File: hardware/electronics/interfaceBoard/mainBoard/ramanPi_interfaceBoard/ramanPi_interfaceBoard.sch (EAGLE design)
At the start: 10 parts

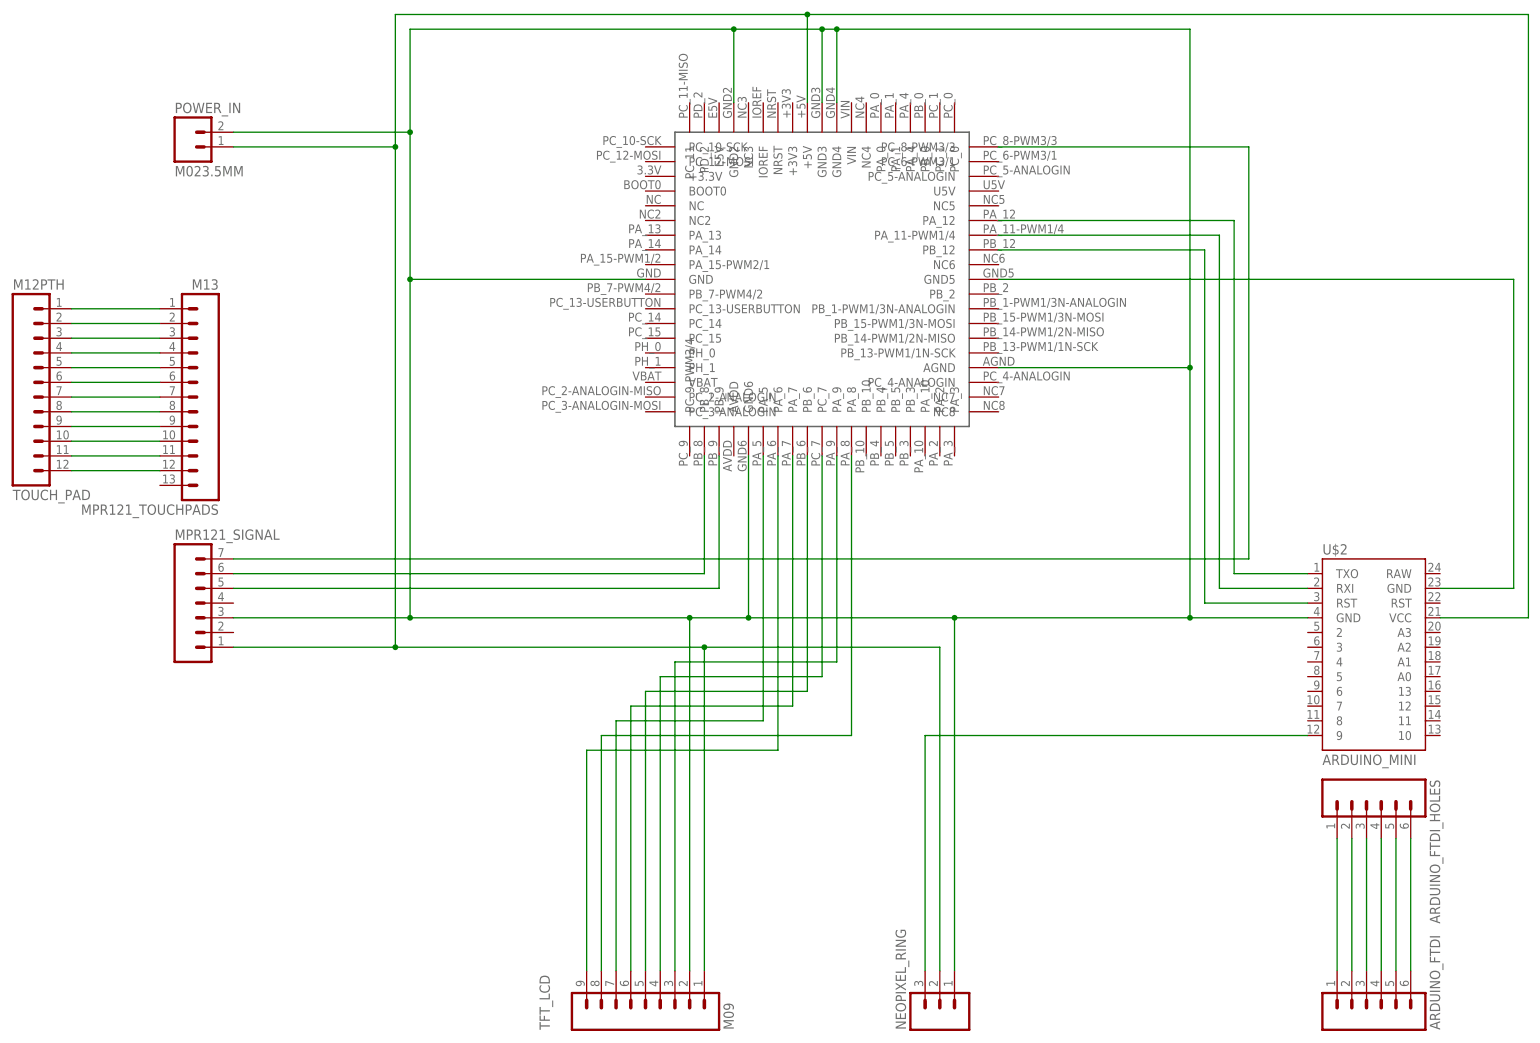
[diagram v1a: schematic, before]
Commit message: added reset circuitry to all stm32 boards
added reset circuitry for raspi to reset each board from remote.
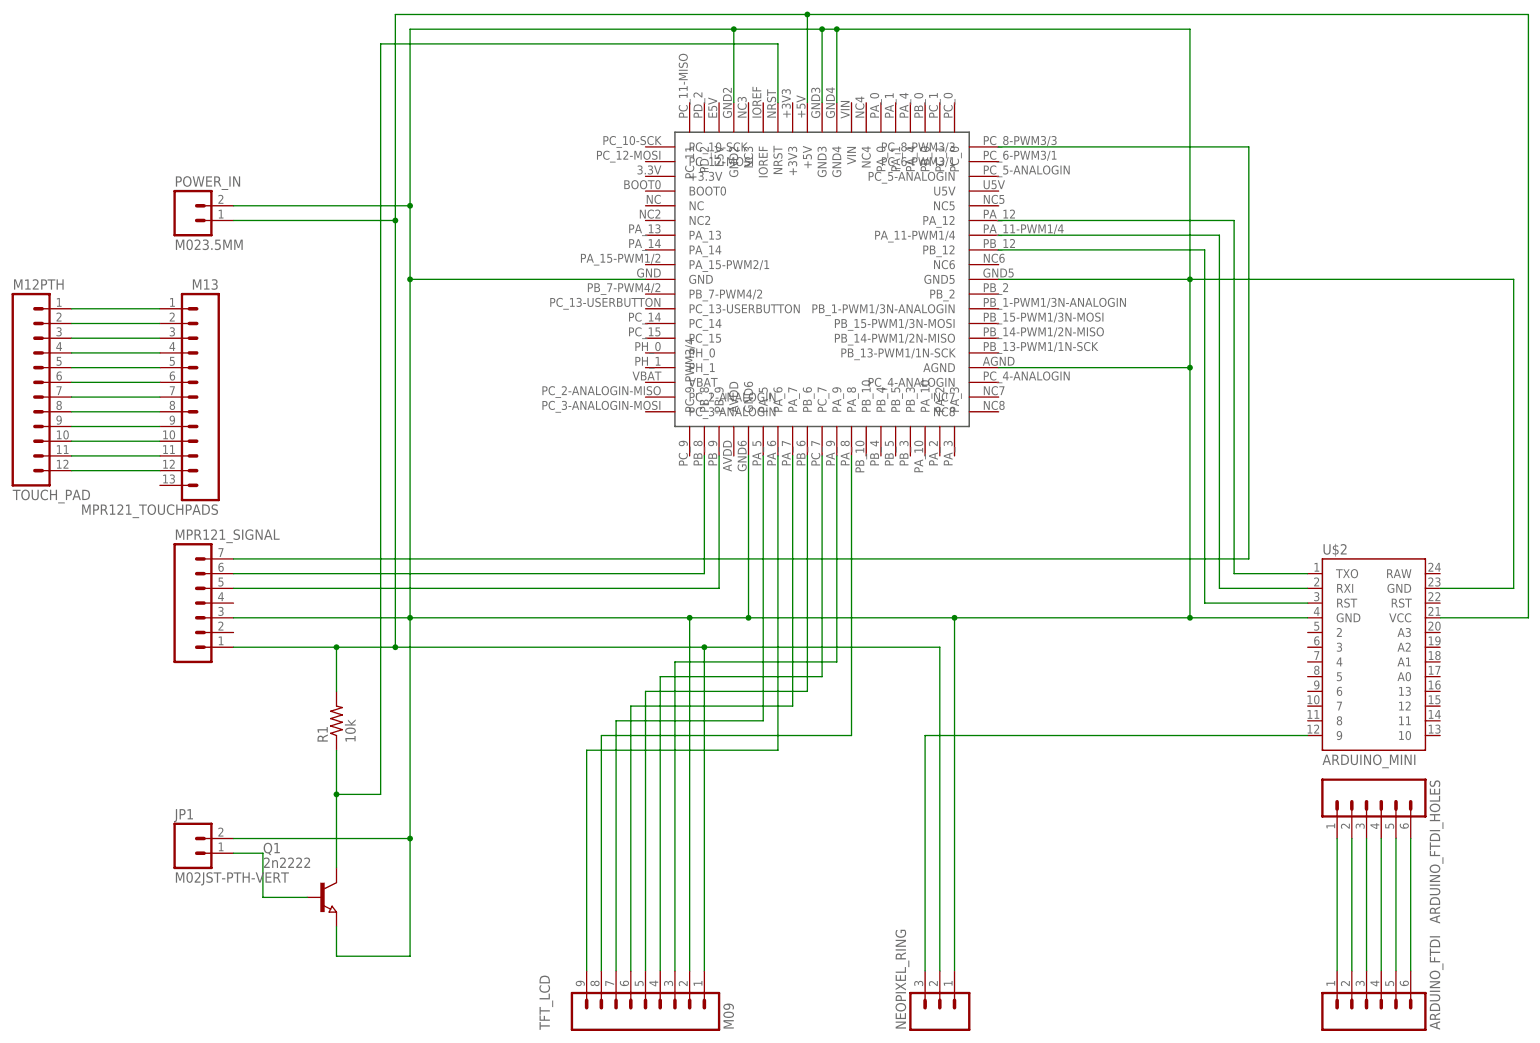
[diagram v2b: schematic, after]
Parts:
- added JP1: M02JST-PTH-VERT, SparkFun-Connectors:M02JST-PTH-VERT
- added Q1: 2n2222, semicon-smd-ipc:NPN-TRANSISTOR_SOT23
- added R1: 10k, adafruit:R-US_M1206
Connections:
- removed net N$1: MPR121_SIGNAL.1, NEOPIXEL_RING.2, POWER_IN.1, TFT_LCD.1, U$1.+5V, U$2.VCC
- removed net N$25: MPR121_SIGNAL.3, NEOPIXEL_RING.1, POWER_IN.2, TFT_LCD.2, U$1.AGND, U$1.GND, U$1.GND2, U$1.GND3, U$1.GND4, U$1.GND5, U$1.GND6, U$2.GND, U$2.GND@2
- new net +5V: MPR121_SIGNAL.1, NEOPIXEL_RING.2, POWER_IN.1, R1.2, TFT_LCD.1, U$1.+5V, U$2.VCC
- new net GND: JP1.2, MPR121_SIGNAL.3, NEOPIXEL_RING.1, POWER_IN.2, Q1.E, TFT_LCD.2, U$1.AGND, U$1.GND, U$1.GND2, U$1.GND3, U$1.GND4, U$1.GND5, U$1.GND6, U$2.GND, U$2.GND@2
- new net N$35: Q1.C, R1.1, U$1.NRST
- new net N$36: JP1.1, Q1.B
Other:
- moved on the sheet: POWER_IN
